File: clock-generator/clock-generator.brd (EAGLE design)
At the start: 50 x 100 mm, 85 parts, among them IC1 24C00TS, K2 694108106102, M1 MENTOR_12701001, U1 SN74LVC1G04DBV, U3 ATSAMD11-QFN24, U4 SI5351C, U5 IP4234CZ6, U6 IP4234CZ6, U7 VCTCXO-CONNORWINFIELD, X1 MINI-USB-SHIELD-UX60A-MB-5ST, X2 JACK2.5_SJ-2523, X4 UEXT/90

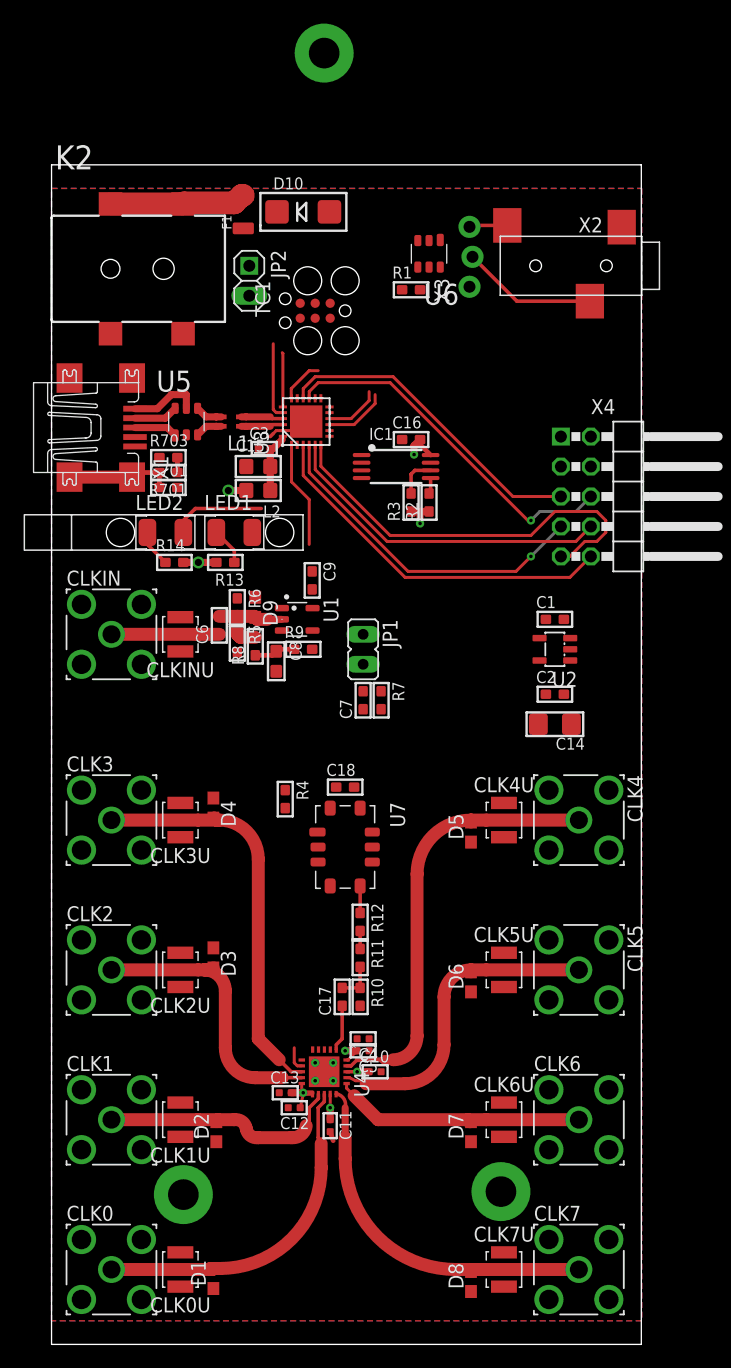
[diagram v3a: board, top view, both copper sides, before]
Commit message: clock-gen: finish routing of PCB layout
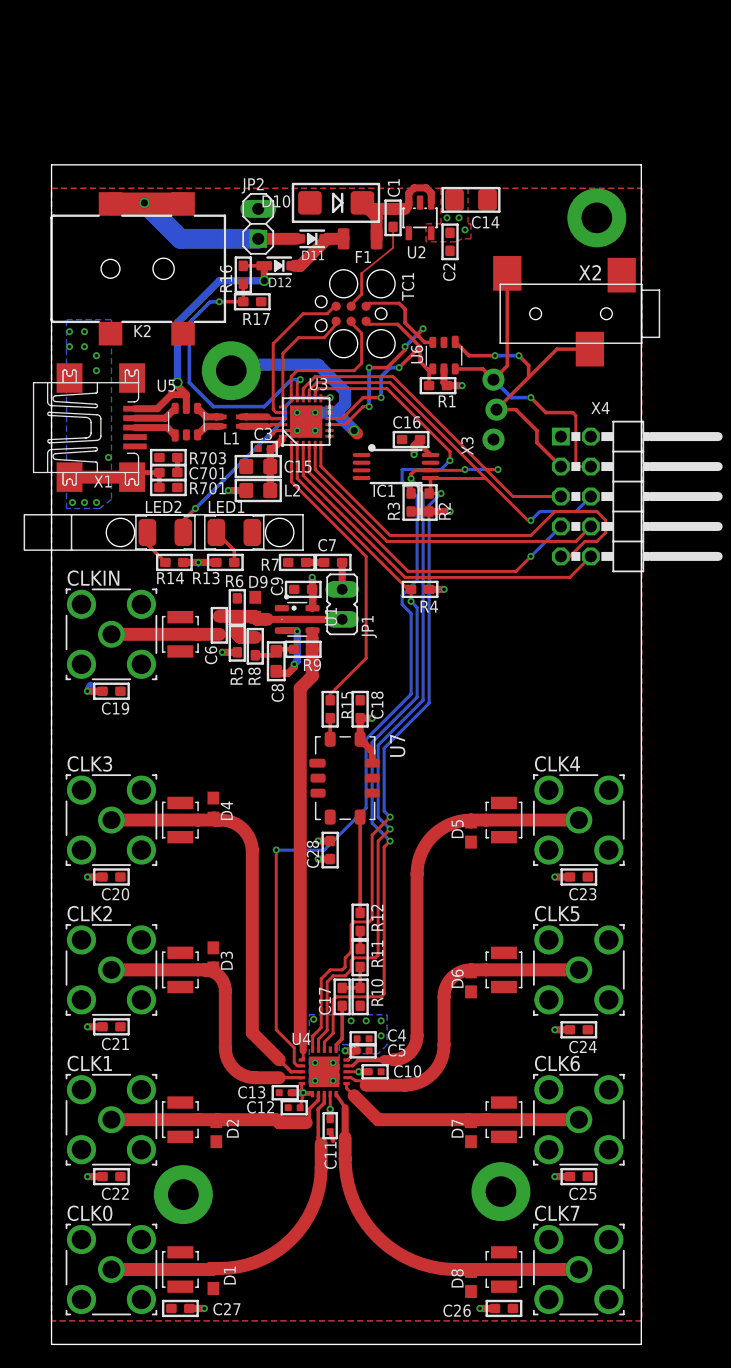
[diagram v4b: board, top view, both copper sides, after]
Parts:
- added C19, C20, C21, C22, C23, C24, C25, C26, C27, C28: 100n, rc-sysmocom:_0603
- added D11, D12: CUS08F30, diodes-sysmocom:SOD-323
- added R15: 33, rc-sysmocom:_0603
- added R16: 30k, rc-sysmocom:_0603
- added R17: 47k, rc-sysmocom:_0603
- moved C14 45.0 mm to (35.6, 97.0)
- moved C2 39.4 mm to (33.8, 93.5), turned to 270 degrees
- moved U2 38.3 mm to (31.2, 95.5), turned to 180 degrees
- moved C1 36.7 mm to (29.0, 95.5), turned to 90 degrees
- moved R4 21.1 mm to (31.2, 64.0), turned to 180 degrees
- moved R7 13.7 mm to (20.8, 66.3), turned to 0 degrees
- moved X3 13.1 mm to (37.6, 76.7)
- moved C7 12.0 mm to (23.9, 66.3), turned to 0 degrees
- moved F1 10.2 mm to (26.2, 93.7), turned to 180 degrees
- moved U6 8.73 mm to (33.3, 83.8)
- moved R1 8.44 mm to (32.8, 81.3)
- moved C18 6.73 mm to (26.2, 53.8), turned to 270 degrees
- moved U7 5.84 mm to (24.9, 48.0)
- moved JP2 4.89 mm to (17.5, 95.0), turned to 90 degrees
- moved JP1 4.20 mm to (24.6, 62.7), turned to 0 degrees
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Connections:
- removed net N$8: U6.1, X2.3, X3.2
- removed net N$9: C18.2, U7.9
- removed net VCTCXO_EN: U7.8
- new net UART_RX0: U6.6, X2.2, X3.3, X4.4
- new net UART_TX0: U6.1, X2.3, X3.2, X4.3
- new net VCXO_CV: R15.1, U3.1
- net !INT: now also U3.2; no longer U3.1
- net GND: now also C19.1, C20.1, C21.1, C22.1, C23.1, C24.1, C25.1, C26.1, C27.1, R17.1
- net N$10: now also R15.2
- net N$15: now also D11.A; no longer F1.2
- net N$6: now also D11.C, D12.C, F1.2; no longer U6.6, X2.2, X3.3
- net UART_RX: no longer X4.4
- net UART_TX: no longer X4.3
- net VBUS: now also D12.A, R16.2
- net VBUS_DET: now also R16.1, R17.2
- net VDD: now also C18.2, C19.2, C20.2, C21.2, C22.2, C23.2, C24.2, C25.2, C26.2, C27.2, C28.1, C28.2, U7.8, U7.9
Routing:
- net !OEB: track 2.02 -> 79.6 mm, vias 0 -> 2
- net I2C_SCL: track 30.7 -> 92.4 mm, vias 0 -> 4
- net I2C_SDA: track 31.8 -> 92.3 mm, vias 1 -> 3
- net !INT: track 9.06 -> 62.4 mm, vias 0 -> 2
- net CLKIN_CMOS: track 0.00 -> 37.0 mm
- net GND: track 4.38 -> 41.3 mm, vias 7 -> 30
- net VDD: track 23.1 -> 52.8 mm, vias 8 -> 27
- net UART_RX0: track 0.00 -> 26.8 mm, vias 0 -> 1
- net UART_TX0: track 0.00 -> 26.2 mm, vias 0 -> 2
- net VCXO_CV: track 0.00 -> 25.5 mm
- net VBUS_DET: track 0.00 -> 24.8 mm, vias 0 -> 2
- net VBUS: track 6.01 -> 24.3 mm, vias 0 -> 2
- net UART_TX: track 5.37 -> 21.9 mm, vias 0 -> 4
- net UART_RX: track 4.75 -> 20.8 mm, vias 0 -> 2
- net N$15: track 11.6 -> 23.9 mm, vias 0 -> 1
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- added copper zone on layer 16, net GND
- added copper zone on layer 1, net VDD

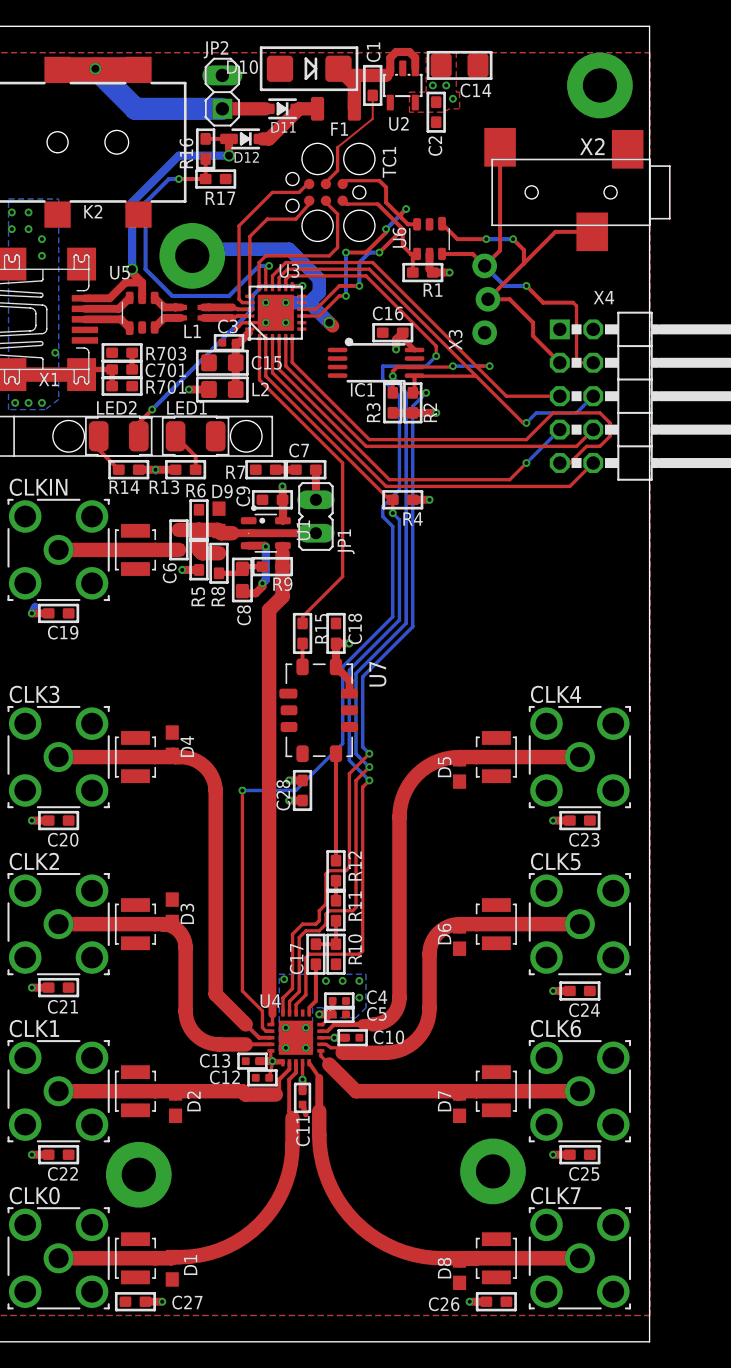
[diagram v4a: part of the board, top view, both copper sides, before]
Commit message: clock-gen: Cosmetic changes
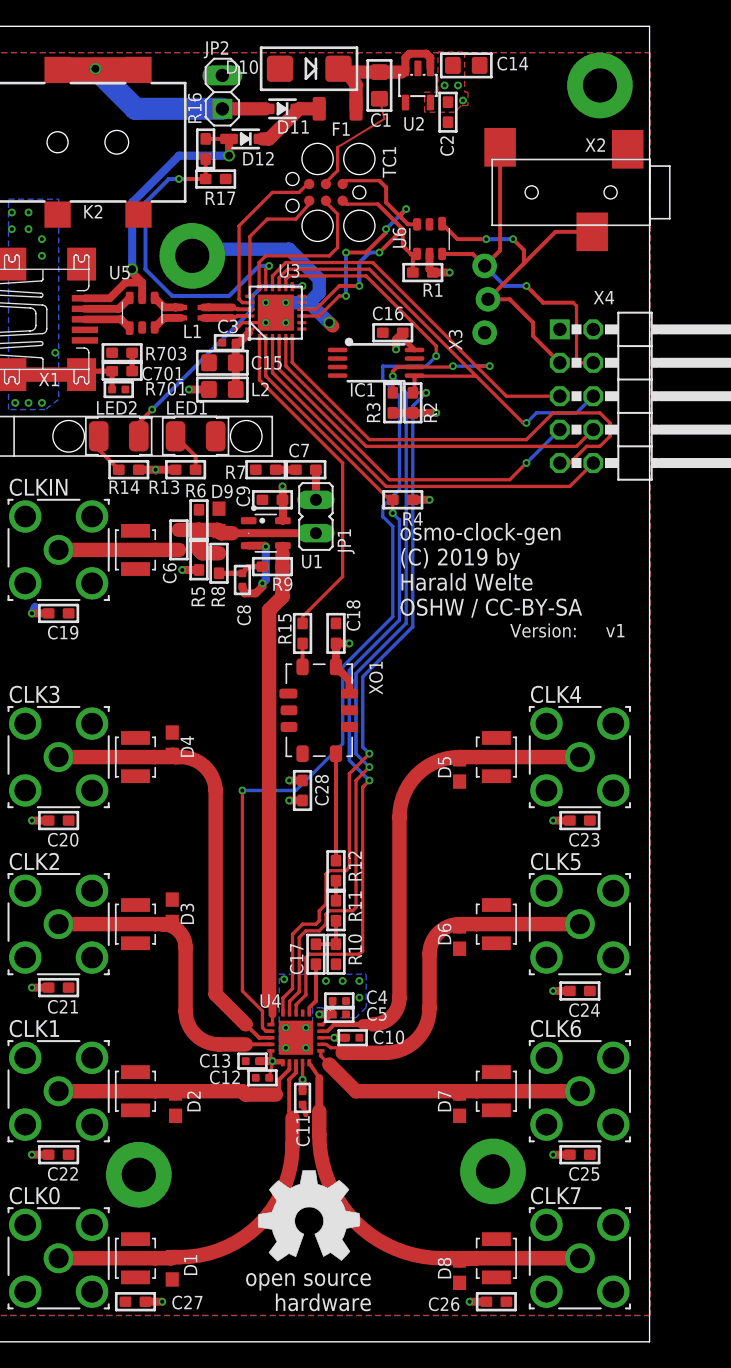
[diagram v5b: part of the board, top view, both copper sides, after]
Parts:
- added U$1: (no value), oshw:OSHW_8MM
- C1: value 1uF -> 4.7u; device rc-sysmocom:_0603 -> rc-sysmocom:_0805
- C10, C11, C12, C13: value 0.01uF -> 10n
- C14: value (none) -> 4.7u; device rc-sysmocom:1206 -> rc-sysmocom:_0805
- C2: value 0.01uF -> 100n
- C4: value 1uF -> 1u
- C5: value 0.01uF -> 0.10n
- C701: device rc-sysmocom:_0603 -> rc-sysmocom:_0402
- C8: device rc-sysmocom:0603 -> rc-sysmocom:_0402
- U2: value (none) -> ADP151AUJZ
- moved U2 1.15 mm to (32.4, 95.5)
- moved C2 0.89 mm to (34.7, 93.5)
- moved C1 0.51 mm to (29.5, 95.5)
- moved C14 0.51 mm to (36.1, 97.0)
- moved C701 0.36 mm to (9.65, 72.4)
- moved F1 0.13 mm to (26.3, 93.7)
- moved R701 0.13 mm to (9.91, 73.8)
- renumbered U7 to XO1
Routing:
- net N$14: track 11.2 -> 12.1 mm
- net GND: track 41.3 -> 42.2 mm
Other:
- board text added: ">REVISION"
- board text added: "Version:"
- board text added: "osmo-clock-gen (C) 2018 by Harald Welte OSHW / CC-BY-SA"
- board text added: "osmo-clock-gen (C) 2019 by Harald Welte OSHW / CC-BY-SA"

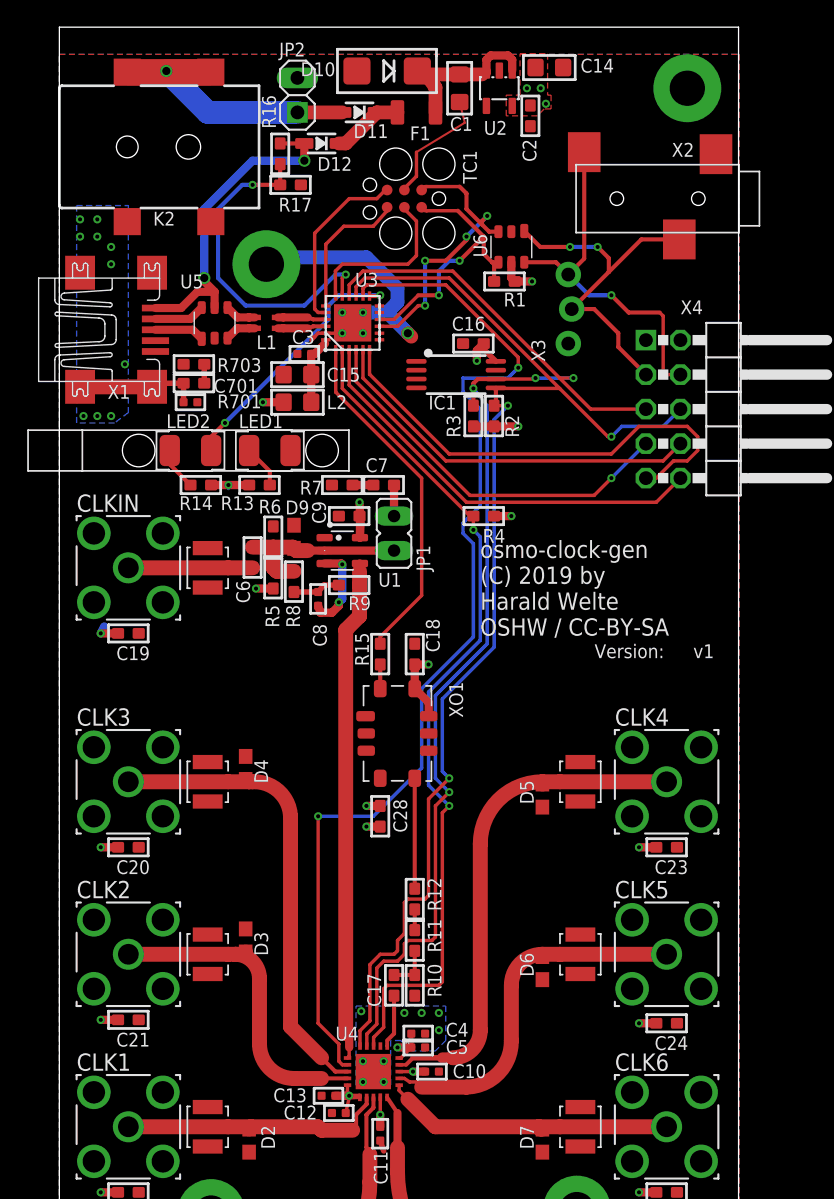
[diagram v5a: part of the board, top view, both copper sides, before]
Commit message: clock-gen: Minor changes; final version as ordered
* move DC jack to extend beyond PCB edge into front panel
* harmonize component variants (10n only 0402, 4.7u only 0805)
* add "sysmocom" as manufacturer name (WEEE requirement)
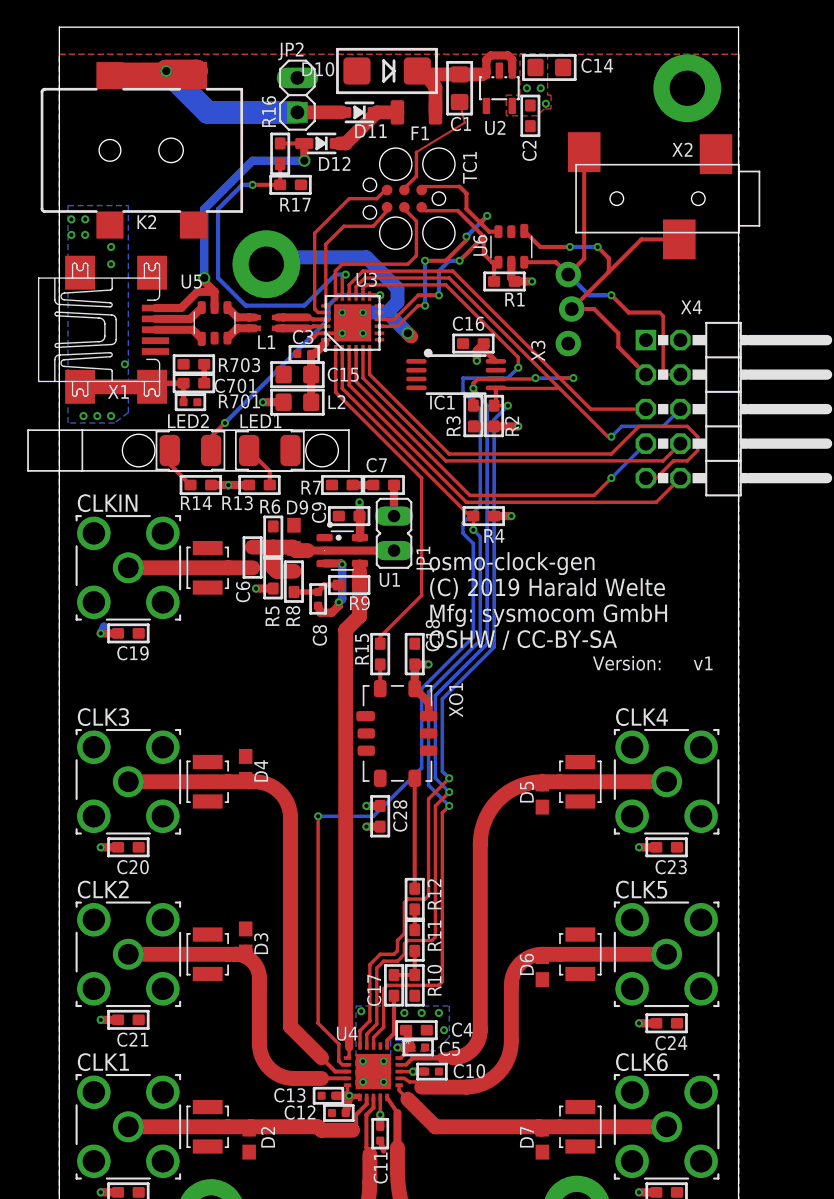
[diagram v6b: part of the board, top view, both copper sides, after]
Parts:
- C4: device rc-sysmocom:_0402 -> rc-sysmocom:_0603
- moved K2 1.30 mm to (-1.27, 90.9)
- moved C4 0.29 mm to (26.3, 26.2)
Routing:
- net N$15: track 23.9 -> 23.0 mm
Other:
- board text added: "osmo-clock-gen (C) 2019 Harald Welte Mfg: sysmocom GmbH OSHW / CC-BY-SA"
- board text added: "osmo-clock-gen (C) 2019 by Harald Welte Mfg: sysmocom GmbH OSHW / CC-BY-SA"
- board text removed: "osmo-clock-gen (C) 2018 by Harald Welte OSHW / CC-BY-SA"
- board text removed: "osmo-clock-gen (C) 2019 by Harald Welte OSHW / CC-BY-SA"

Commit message: clock-gen: Add BOM information + PDF exports of schematics
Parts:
- C5: value 0.10n -> 10n
- D10: value DIODDE-ZENER-SMA -> 5.6V
- F1: value (none) -> 200mA

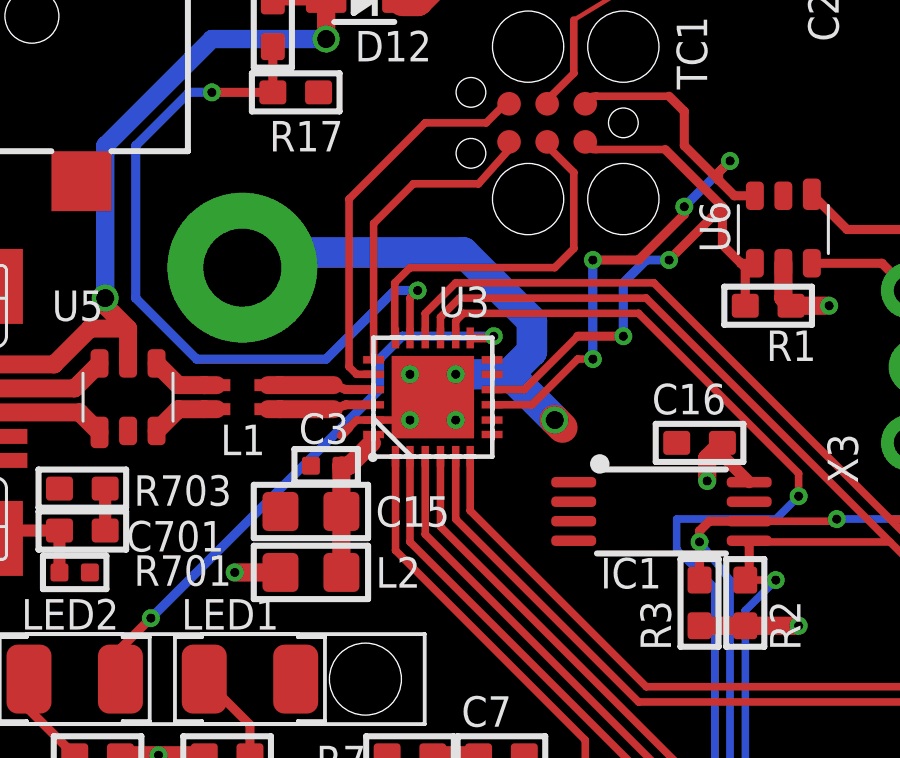
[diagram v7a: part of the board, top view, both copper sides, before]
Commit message: WIP: click-generator: Replace U3 (so far SAMD11) with SAMD21
Closes: OS#3856
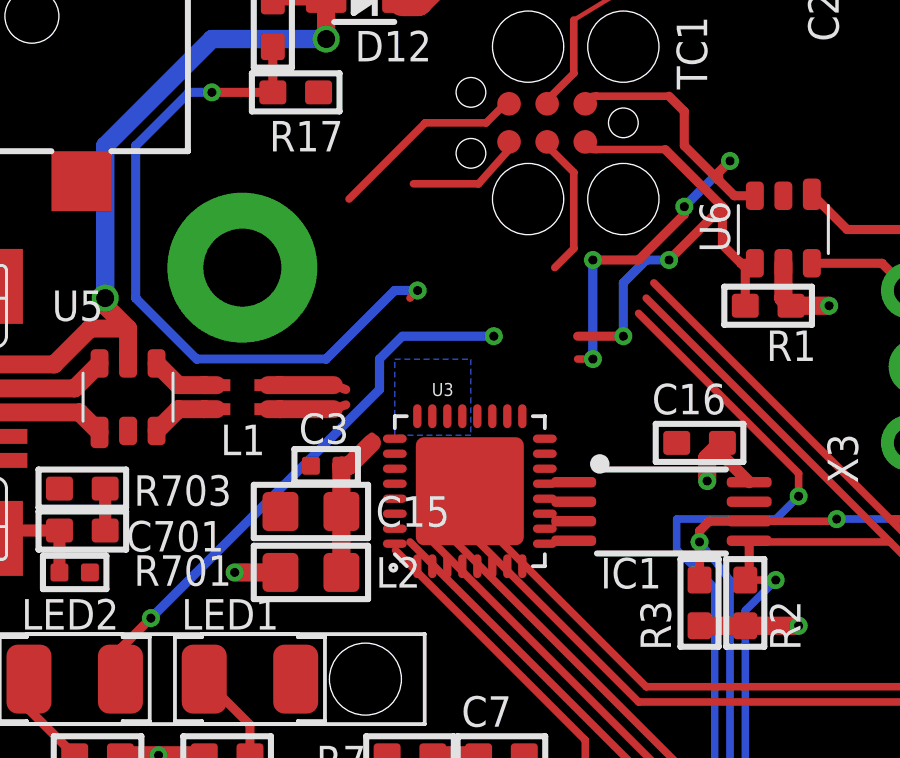
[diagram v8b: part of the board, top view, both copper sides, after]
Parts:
- U3: value ATSAMD11-QFN24 -> ATSAMD21E; device atmel-arm:QFN24_4X4 -> atmel-arm:QFN32_5X5
- moved U3 3.37 mm to (22.8, 75.1), turned to 0 degrees
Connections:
- net !INT: now also U3.4; no longer U3.2
- net !LED_YELLOW: now also U3.17; no longer U3.13
- net !OEB: now also U3.18; no longer U3.14
- net !RESET: now also U3.26; no longer U3.18
- net !SPI_SS: now also U3.6; no longer U3.3
- net GND: now also U3.10, U3.28, U3.EXP; no longer U3.23, U3.25
- net I2C_SCL: now also U3.12; no longer U3.16
- net I2C_SDA: now also U3.11; no longer U3.15
- net N$13: no longer U3.24
- net SPI_MISO: now also U3.5; no longer U3.4
- net SPI_MOSI: now also U3.7; no longer U3.5
- net SPI_SCK: now also U3.8; no longer U3.6
- net SWCLK: now also U3.31; no longer U3.19
- net SWDIO: now also U3.32; no longer U3.20
- net UART_RX: now also U3.22; no longer U3.10
- net UART_TX: now also U3.21; no longer U3.9
- net USB_D_N: now also U3.23; no longer U3.21
- net USB_D_P: now also U3.24; no longer U3.22
- net VBUS_DET: now also U3.25; no longer U3.17
- net VCXO_CV: now also U3.3; no longer U3.1
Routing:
- net GND: track 42.2 -> 17.4 mm, vias 30 -> 25
- net I2C_SCL: track 92.4 -> 83.5 mm
- net I2C_SDA: track 92.3 -> 84.5 mm
- net !RESET: track 12.2 -> 4.82 mm
- net !OEB: track 79.6 -> 72.8 mm
- net SWDIO: track 13.2 -> 6.65 mm
- net SWCLK: track 10.4 -> 3.96 mm
- net UART_RX: track 20.8 -> 17.2 mm
- net UART_TX: track 21.9 -> 18.5 mm
- net VCXO_CV: track 25.5 -> 22.4 mm
- net !INT: track 62.4 -> 59.5 mm
- net !SPI_SS: track 31.3 -> 28.7 mm
- net SPI_MISO: track 28.7 -> 26.4 mm
- net SPI_MOSI: track 28.5 -> 26.4 mm
- net SPI_SCK: track 35.2 -> 33.4 mm
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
